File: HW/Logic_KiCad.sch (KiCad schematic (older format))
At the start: 35 parts, among them Q10 Q_NMOS_GSD, Q11 Q_NMOS_GSD, Q3 Q_NMOS_GSD, SW1 SW_SPDT, SW13 SW_SPST, SW14 SW_SPST, SW15 SW_SPST, U1 ESP32-PICO-D4

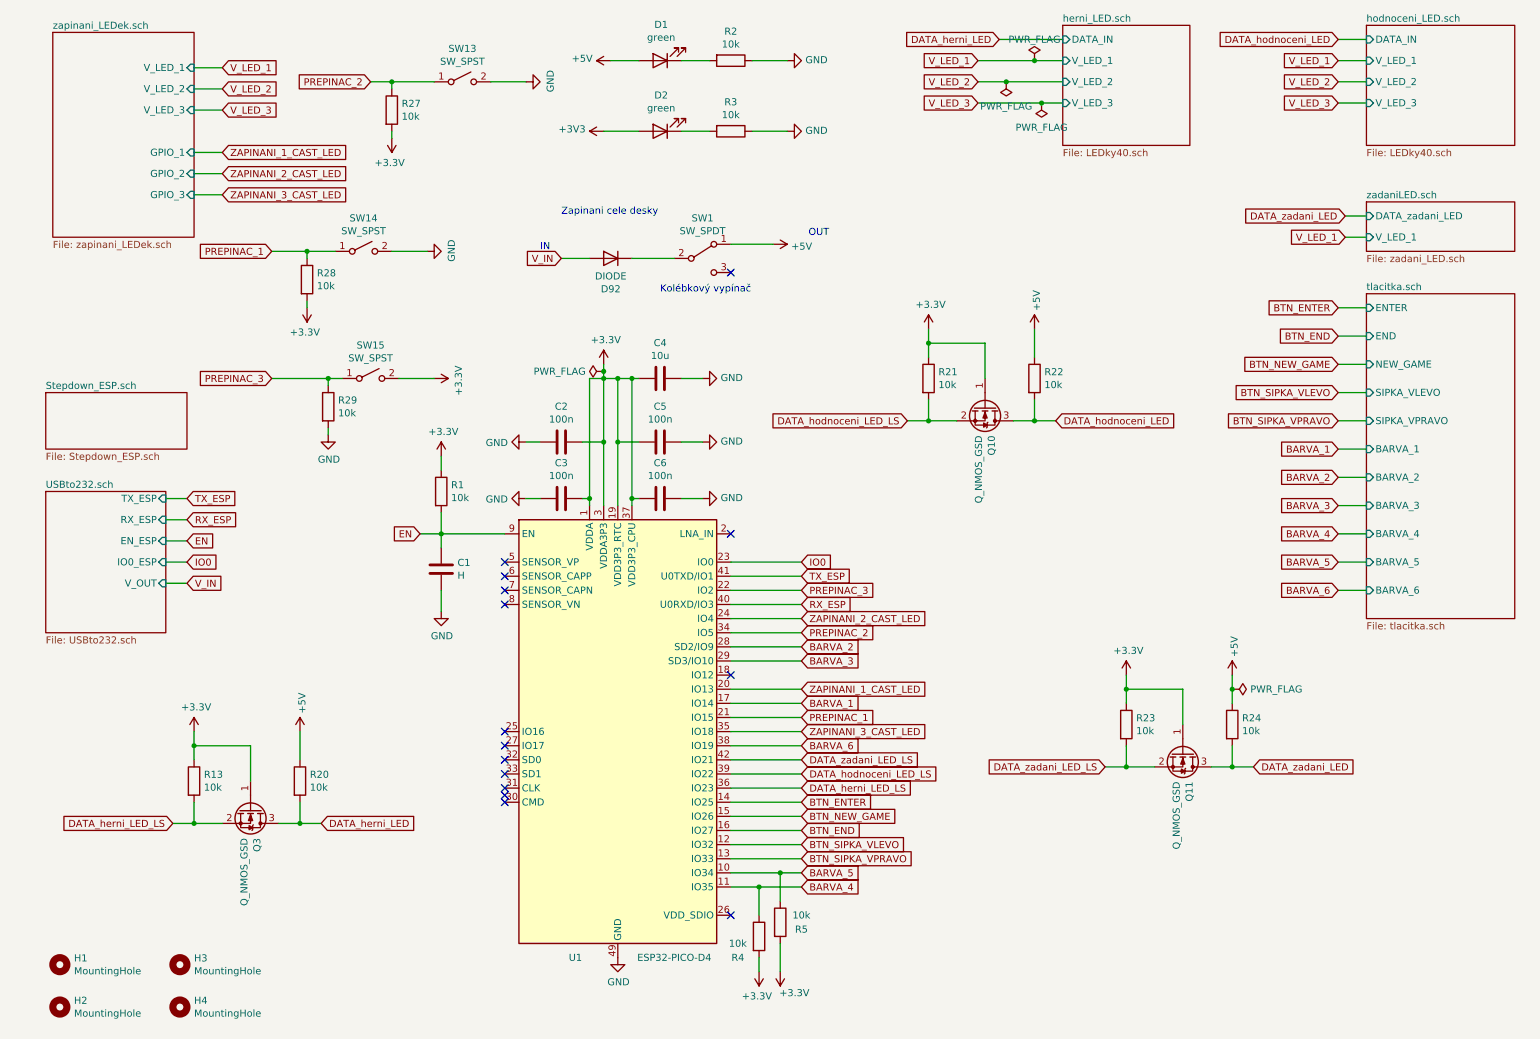
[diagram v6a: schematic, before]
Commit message: make schematic beautiful (for printing)
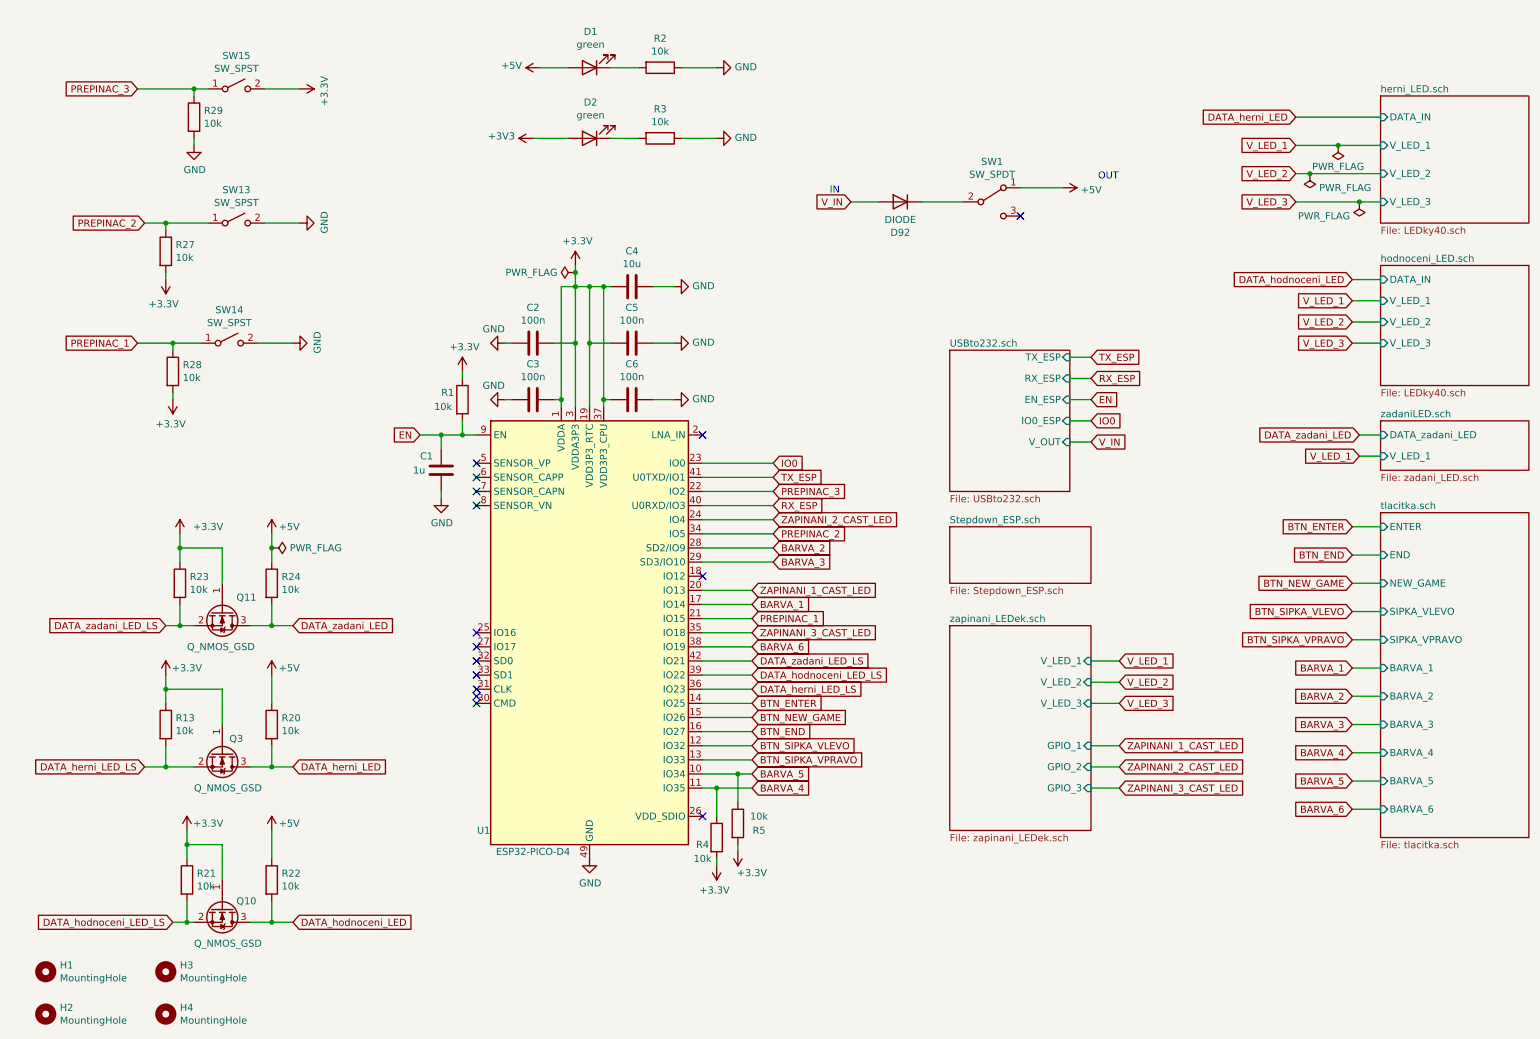
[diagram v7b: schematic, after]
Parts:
- C1: value H -> 1u
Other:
- note removed: "Kolébkový vypínač"
- note removed: "Zapinani cele desky\n"
- moved on the sheet: C1, C2, C3, C4, C5, C6, D1, D2, D92, H1, H2, H3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
